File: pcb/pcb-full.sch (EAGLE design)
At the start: 125 parts, among them IC1 STM32F401RET6U, IC2 LDS3985M33R, IC3 LDS3985M33R, IC4 HX711, IC5 TLV2462IP, J12 B2B-PH-K-S_LF__SN_, J14 3V3 LED, J15 VDDA LED, J16 HX711 LED, J18 DC Power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

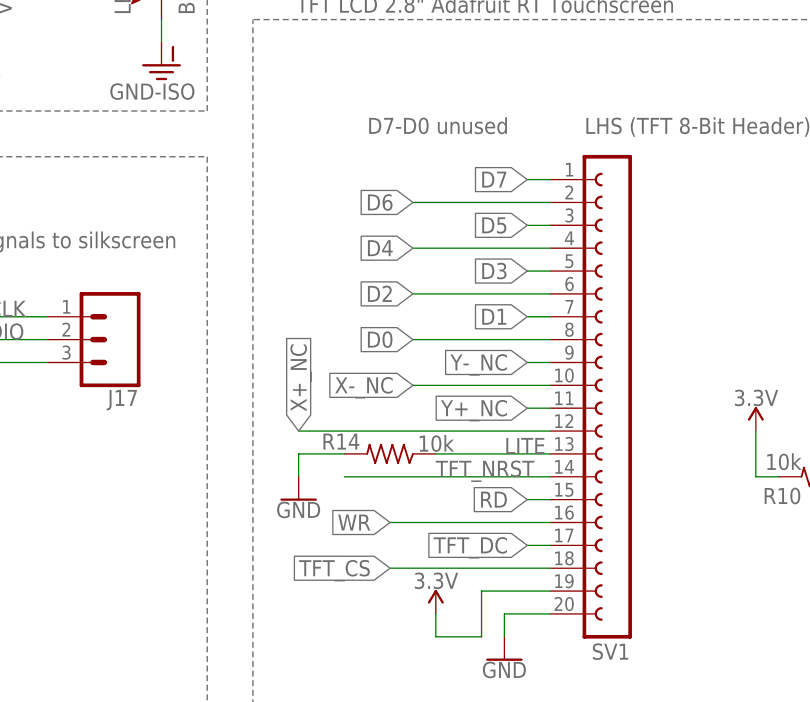
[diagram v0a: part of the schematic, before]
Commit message: Updated the 8 mil trace clearance and DRC
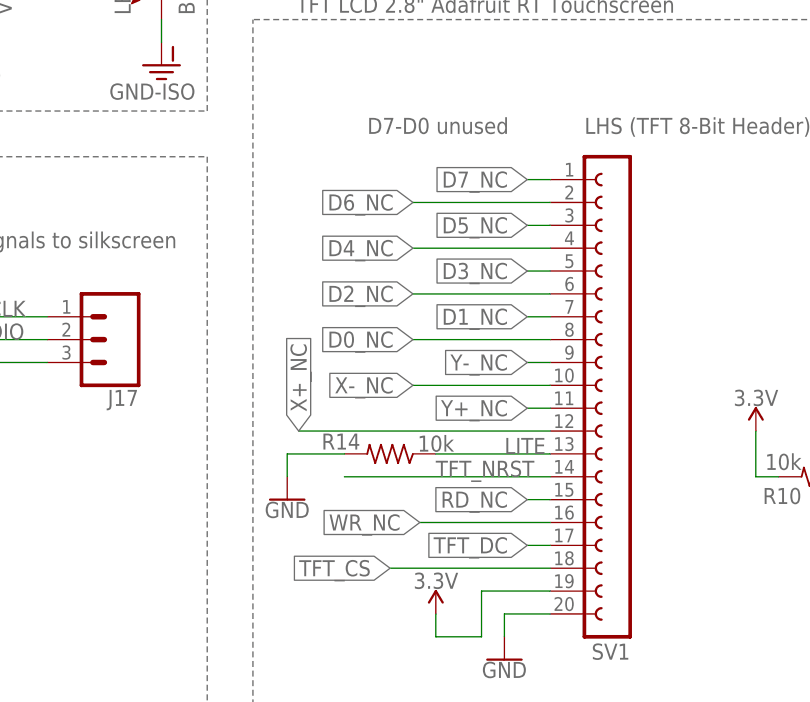
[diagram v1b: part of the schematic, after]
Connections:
- net D0 renamed D0_NC
- net D1 renamed D1_NC
- net D2 renamed D2_NC
- net D3 renamed D3_NC
- net D4 renamed D4_NC
- net D5 renamed D5_NC
- net D6 renamed D6_NC
- net D7 renamed D7_NC
- net RD renamed RD_NC
- net WR renamed WR_NC
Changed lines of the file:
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@@
 <setting verticaltext="up"/>
 </settings>
-<grid distance="0.1" unitdist="inch" unit="inch" style="lines" multiple="1" display="no" altdistance="0.01" altunitdist="inch" altunit="inch"/>
+<grid distance="0.1" unitdist="inch" unit="inch" style="lines" multiple="1" display="yes" altdistance="0.01" altunitdist="inch" altunit="inch"/>
 <layers>
 <layer number="1" name="Top" color="4" fill="1" visible="no" active="no"/>
@@
 <attribute name="VALUE" x="351.536" y="46.101" size="1.778" layer="96"/>
 </instance>
-<instance part="GND55" gate="G$1" x="182.88" y="121.92" smashed="yes">
-<attribute name="VALUE" x="182.88" y="121.666" size="1.778" layer="96" align="top-center"/>
+<instance part="GND55" gate="G$1" x="181.61" y="121.92" smashed="yes">
+<attribute name="VALUE" x="181.61" y="121.666" size="1.778" layer="96" align="top-center"/>
 </instance>
 <instance part="SUPPLY12" gate="VDD" x="344.17" y="63.5" smashed="yes">
@@
 <pinref part="GND55" gate="G$1" pin="GND"/>
 <pinref part="R14" gate="G$1" pin="2"/>
-<wire x1="182.88" y1="124.46" x2="182.88" y2="127" width="0.1524" layer="91"/>
-<wire x1="182.88" y1="127" x2="187.96" y2="127" width="0.1524" layer="91"/>
+<wire x1="181.61" y1="124.46" x2="181.61" y2="127" width="0.1524" layer="91"/>
+<wire x1="181.61" y1="127" x2="187.96" y2="127" width="0.1524" layer="91"/>
 </segment>
 <segment>
@@
 </segment>
 </net>
-<net name="D7" class="0">
+<net name="D7_NC" class="0">
 <segment>
 <pinref part="SV1" gate="G$1" pin="1"/>
@@
 </segment>
 </net>
-<net name="D6" class="0">
+<net name="D6_NC" class="0">
 <segment>
 <pinref part="SV1" gate="G$1" pin="2"/>
@@
 </segment>
 </net>
-<net name="D5" class="0">
+<net name="D5_NC" class="0">
 <segment>
 <pinref part="SV1" gate="G$1" pin="3"/>
@@
 </segment>
 </net>
-<net name="D4" class="0">
+<net name="D4_NC" class="0">
 <segment>
 <pinref part="SV1" gate="G$1" pin="4"/>
@@
 </segment>
 </net>
-<net name="D3" class="0">
+<net name="D3_NC" class="0">
 <segment>
 <pinref part="SV1" gate="G$1" pin="5"/>
@@
 </segment>
 </net>
-<net name="D2" class="0">
+<net name="D2_NC" class="0">
 <segment>
 <pinref part="SV1" gate="G$1" pin="6"/>
@@
 </segment>
 </net>
-<net name="D1" class="0">
+<net name="D1_NC" class="0">
 <segment>
 <pinref part="SV1" gate="G$1" pin="7"/>
@@
 </segment>
 </net>
-<net name="D0" class="0">
+<net name="D0_NC" class="0">
 <segment>
 <pinref part="SV1" gate="G$1" pin="8"/>
@@
 </segment>
 </net>
-<net name="RD" class="0">
+<net name="RD_NC" class="0">
 <segment>
 <pinref part="SV1" gate="G$1" pin="15"/>
@@
 </segment>
 </net>
-<net name="WR" class="0">
+<net name="WR_NC" class="0">
 <segment>
 <pinref part="SV1" gate="G$1" pin="16"/>
-<wire x1="210.82" y1="119.38" x2="193.04" y2="119.38" width="0.1524" layer="91"/>
-<label x="193.04" y="119.38" size="1.778" layer="95" rot="R180" xref="yes"/>
-</segment>
-</net>
+<wire x1="210.82" y1="119.38" x2="196.342" y2="119.38" width="0.1524" layer="91"/>
+<label x="196.342" y="119.38" size="1.778" layer="95" rot="R180" xref="yes"/>
+</segment>
+</net>

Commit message: Final version of the PCB? Updated headers + silkscreen + AGND
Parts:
- added R47: 0.1, LinnesLab-Passives:RESISTOR0603
- J3: device LinnesLab-Connectors:CONN_06LOCK -> LinnesLab-Connectors:CONN_06SILK_FEMALE_PTH
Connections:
- net GND-ISO: now also R47.1, R47.2
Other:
- note added: "GND connection"
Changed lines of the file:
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@@
 <setting verticaltext="up"/>
 </settings>
-<grid distance="0.1" unitdist="inch" unit="inch" style="lines" multiple="1" display="yes" altdistance="0.01" altunitdist="inch" altunit="inch"/>
+<grid distance="0.1" unitdist="inch" unit="inch" style="lines" multiple="1" display="no" altdistance="0.01" altunitdist="inch" altunit="inch"/>
 <layers>
 <layer number="1" name="Top" color="4" fill="1" visible="no" active="no"/>
@@
 <part name="R45" library="LinnesLab-Passives" deviceset="RESISTOR" device="0603" package3d_urn="urn:adsk.eagle:package:15661944/2" value="20"/>
 <part name="R46" library="LinnesLab-Passives" deviceset="RESISTOR" device="0603" package3d_urn="urn:adsk.eagle:package:15661944/2" value="20"/>
-<part name="J3" library="LinnesLab-Connectors" deviceset="CONN_06" device="LOCK"/>
 <part name="GND18" library="LinnesLab-Symbols" deviceset="GND" device=""/>
 <part name="SUPPLY41" library="LinnesLab-Symbols" deviceset="3.3V" device=""/>
+<part name="R47" library="LinnesLab-Passives" deviceset="RESISTOR" device="0603" package3d_urn="urn:adsk.eagle:package:15661944/2" value="0.1"/>
+<part name="GND-ISO8" library="LinnesLab-Symbols" deviceset="GND-ISO" device=""/>
+<part name="GND-ISO9" library="LinnesLab-Symbols" deviceset="GND-ISO" device=""/>
+<part name="J3" library="LinnesLab-Connectors" deviceset="CONN_06" device="SILK_FEMALE_PTH"/>
 </parts>
 <sheets>
@@
 <wire x1="256.54" y1="180.34" x2="256.54" y2="215.9" width="0.1524" layer="95" style="shortdash"/>
 <text x="264.16" y="218.44" size="1.778" layer="95">I2C BR24S64J-WE2 EEPROM</text>
+<text x="509.27" y="19.304" size="1.778" layer="95">GND connection</text>
 </plain>
 <instances>
@@
 <attribute name="VALUE" x="114.046" y="143.256" size="1.778" layer="96" rot="R180"/>
 </instance>
-<instance part="J3" gate="G$1" x="20.32" y="78.74" smashed="yes">
-<attribute name="VALUE" x="15.24" y="68.834" size="1.778" layer="96" font="vector"/>
-<attribute name="NAME" x="15.24" y="89.408" size="1.778" layer="95" font="vector"/>
-</instance>
 <instance part="GND18" gate="G$1" x="27.94" y="68.58" smashed="yes">
 <attribute name="VALUE" x="27.94" y="68.326" size="1.778" layer="96" align="top-center"/>
@@
 <attribute name="VALUE" x="30.734" y="86.36" size="1.778" layer="96" rot="R270" align="bottom-center"/>
 </instance>
+<instance part="R47" gate="G$1" x="505.46" y="17.78" smashed="yes">
+<attribute name="NAME" x="501.65" y="19.2786" size="1.778" layer="95"/>
+<attribute name="VALUE" x="501.65" y="14.478" size="1.778" layer="96"/>
+</instance>
+<instance part="GND-ISO8" gate="G$1" x="495.3" y="12.7" smashed="yes">
+<attribute name="VALUE" x="495.046" y="9.144" size="1.778" layer="96" rot="R180" align="top-center"/>
+</instance>
+<instance part="GND-ISO9" gate="G$1" x="515.62" y="12.7" smashed="yes">
+<attribute name="VALUE" x="515.366" y="9.144" size="1.778" layer="96" rot="R180" align="top-center"/>
+</instance>
+<instance part="J3" gate="G$1" x="20.32" y="78.74" smashed="yes">
+<attribute name="VALUE" x="15.24" y="68.834" size="1.778" layer="96" font="vector"/>
+<attribute name="NAME" x="15.24" y="89.408" size="1.778" layer="95" font="vector"/>
+</instance>
 </instances>
 <busses>
@@
 <segment>
 <pinref part="GND18" gate="G$1" pin="GND"/>
-<pinref part="J3" gate="G$1" pin="1"/>
 <wire x1="27.94" y1="71.12" x2="27.94" y2="73.66" width="0.1524" layer="91"/>
 <wire x1="27.94" y1="73.66" x2="25.4" y2="73.66" width="0.1524" layer="91"/>
+<pinref part="J3" gate="G$1" pin="1"/>
 </segment>
 </net>
@@
 <segment>
 <pinref part="SUPPLY41" gate="G$1" pin="3.3V"/>
-<pinref part="J3" gate="G$1" pin="6"/>
 <wire x1="27.94" y1="86.36" x2="25.4" y2="86.36" width="0.1524" layer="91"/>
+<pinref part="J3" gate="G$1" pin="6"/>
 </segment>
 </net>
@@
 <pinref part="GND-ISO7" gate="G$1" pin="GND-ISO"/>
 </segment>
+<segment>
+<pinref part="GND-ISO8" gate="G$1" pin="GND-ISO"/>
+<pinref part="R47" gate="G$1" pin="1"/>
+<wire x1="495.3" y1="15.24" x2="495.3" y2="17.78" width="0.1524" layer="91"/>
+<wire x1="495.3" y1="17.78" x2="500.38" y2="17.78" width="0.1524" layer="91"/>
+</segment>
+<segment>
+<pinref part="R47" gate="G$1" pin="2"/>
+<wire x1="510.54" y1="17.78" x2="515.62" y2="17.78" width="0.1524" layer="91"/>
+<wire x1="515.62" y1="17.78" x2="515.62" y2="15.24" width="0.1524" layer="91"/>
+<pinref part="GND-ISO9" gate="G$1" pin="GND-ISO"/>
+</segment>
 </net>
